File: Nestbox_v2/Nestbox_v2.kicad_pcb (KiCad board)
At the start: 2 copper layers, 85 x 60 mm, 93 parts, among them CON301 Micro_SD_Card, J201 BATT_CONN_01X02, J401 LB_DETECT_CONN_01X04, J402 PIR_CONN_01X04, J403 LB_LED_CONN_01X04, J601 LOAD_CELL_CONN_01X04, J701 RFID_CONN_01X05, P301 RX/TX, P302 TST/RST, P303 DEBUG_3V3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

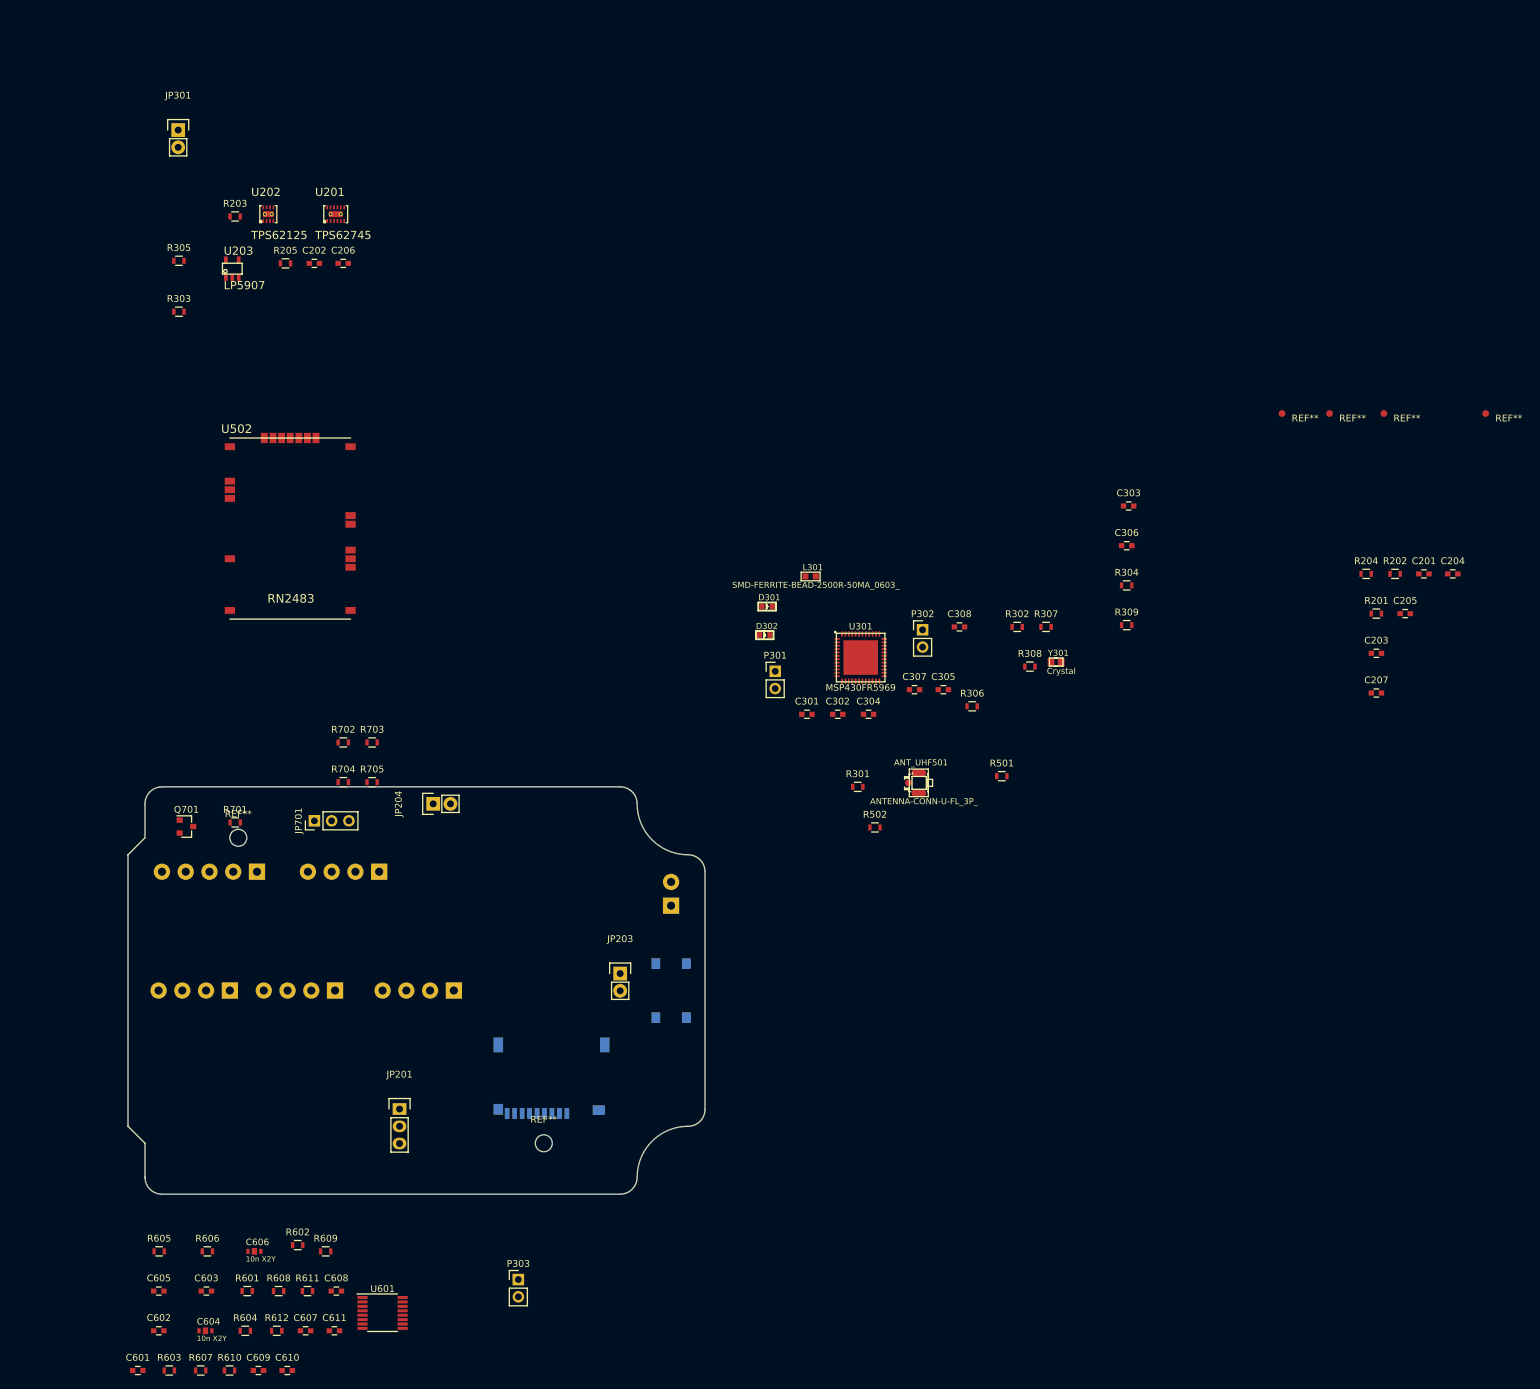
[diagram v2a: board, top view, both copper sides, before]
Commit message: all footprints assigned except mosfets; final connectors and their locatino, started component placement
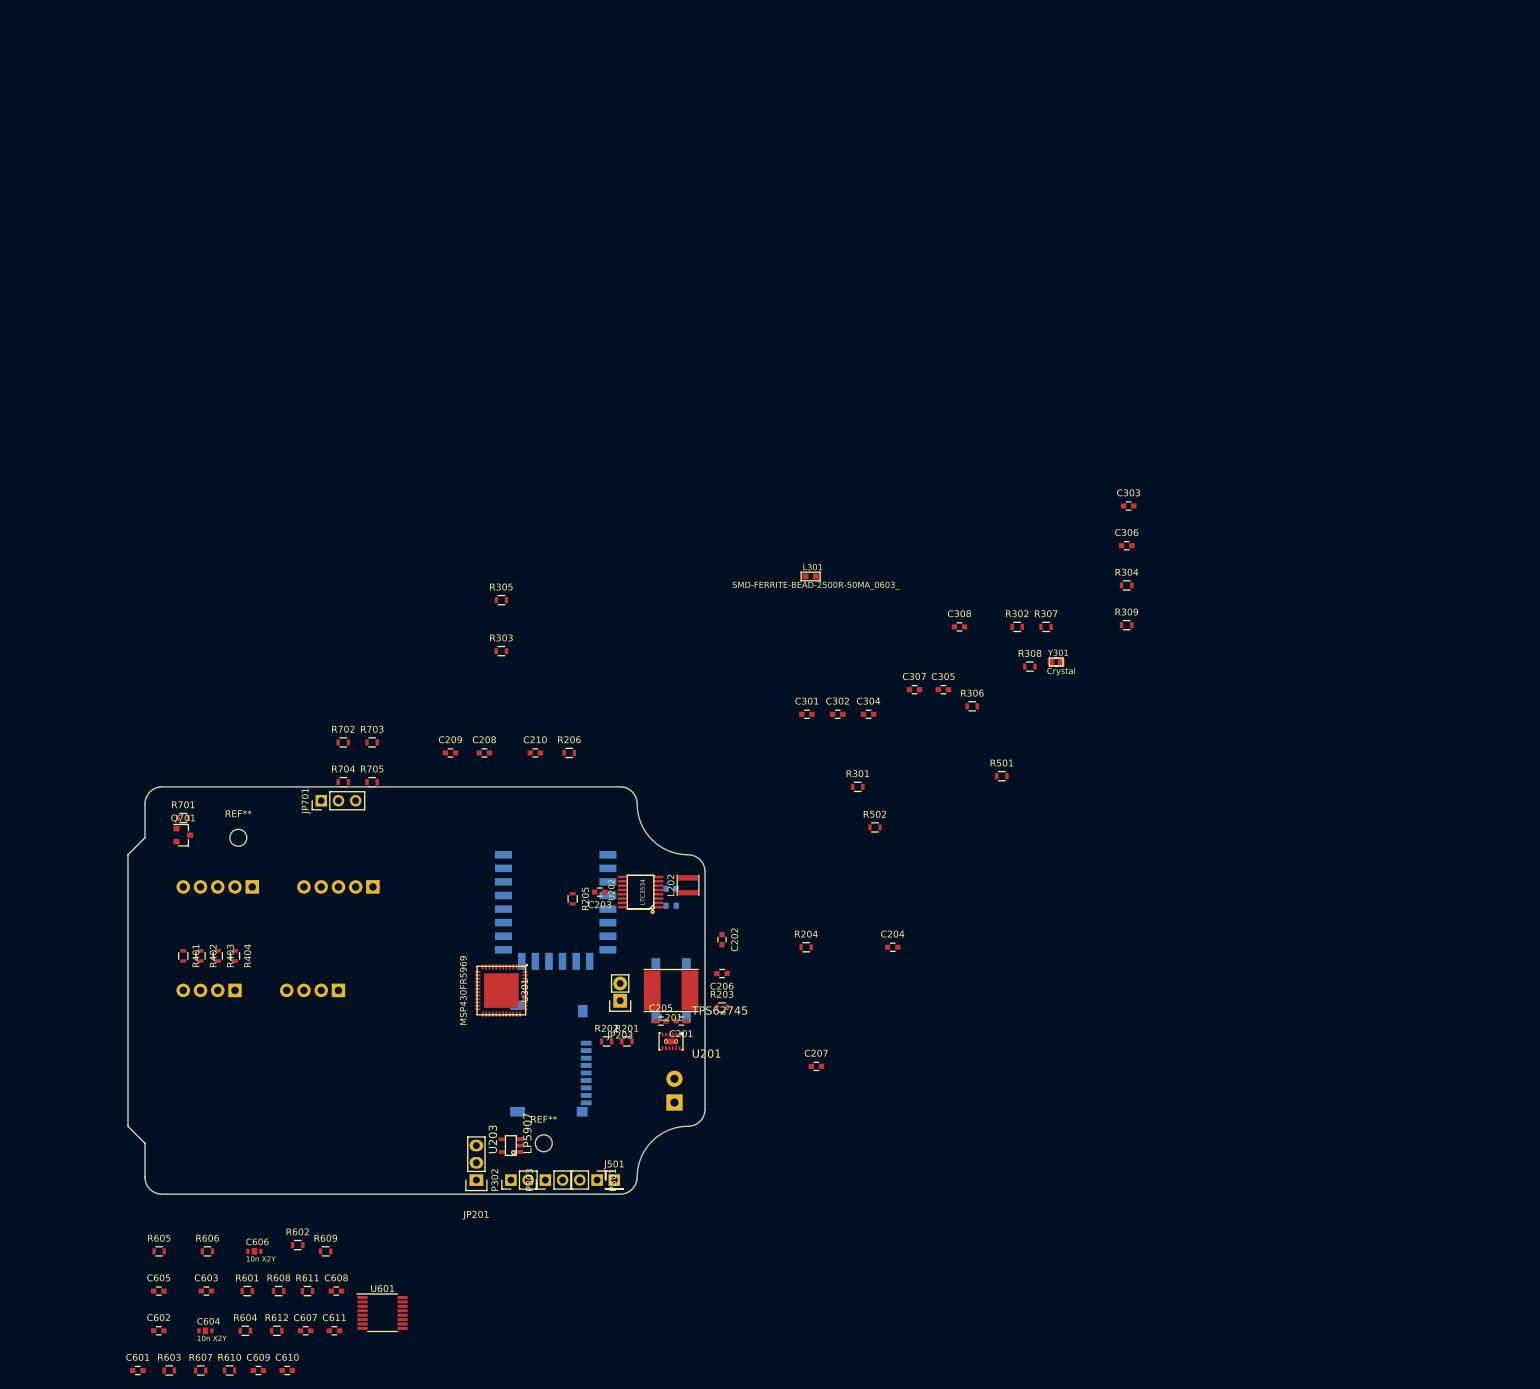
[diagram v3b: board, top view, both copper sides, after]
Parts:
- removed ANT_UHF501: ANTENNA-CONN-U-FL_3P_, SeeedOPL-Connector-2016:U-FL3P-SMD-2.6X2.6X1.0MM
- removed J403: LB_LED_CONN_01X04, Terminal_Blocks:TerminalBlock_Pheonix_PT-3.5mm_4pol
- removed JP204: Jumper_5V, Pin_Headers:Pin_Header_Straight_1x02
- removed JP301: Jumper, Pin_Headers:Pin_Header_Straight_1x02
- removed the REF** at (202.5, 72.5)
- removed the REF** at (209.5, 72.5)
- removed the REF** at (217.5, 72.5)
- removed the REF** at (232.5, 72.5)
- removed U502: RN2483, Octanis3:RN2483
- added C208: 330p, Capacitors_SMD:C_0603, F.Cu at (85.0, 122.5)
- added C209: 10p, Capacitors_SMD:C_0603, F.Cu at (80.0, 122.5)
- added C210: 33p, Capacitors_SMD:C_0603, F.Cu at (92.5, 122.5)
- added J501: CONN_01X01, Pin_Headers:Pin_Header_Straight_1x01_Pitch2.54mm, F.Cu at (104.1, 185.4)
- added L201: 4.7uH, Inductors:Inductor_Taiyo-Yuden_NR-60xx_HandSoldering, F.Cu at (112.5, 157.5)
- added L202: 5uH, Inductors:Inductor_Taiyo-Yuden_NR-30xx, F.Cu at (115.0, 142.0)
- added R206: 15k, Resistors_SMD:R_0603, F.Cu at (97.5, 122.5)
- added R401: DNP, Resistors_SMD:R_0603, F.Cu at (40.6, 152.4)
- added R402: DNP, Resistors_SMD:R_0603, F.Cu at (43.2, 152.4)
- added R403: DNP, Resistors_SMD:R_0603, F.Cu at (45.7, 152.4)
- added R404: DNP, Resistors_SMD:R_0603, F.Cu at (48.3, 152.4)
- added U501: ESP-12S, ESP8266:ESP-12E_SMD, B.Cu at (102.5, 137.5)
- D301, D302: moved to B.Cu
- J401, J601: footprint Terminal_Blocks:TerminalBlock_Pheonix_PT-3.5mm_4pol -> Terminal_Blocks:TerminalBlock_Pheonix_MPT-2.54mm_4pol
- J402: value PIR_CONN_01X04 -> CONN_01X05; footprint Terminal_Blocks:TerminalBlock_Pheonix_PT-3.5mm_4pol -> Terminal_Blocks:TerminalBlock_Pheonix_MPT-2.54mm_5pol
- J701: footprint Terminal_Blocks:TerminalBlock_Pheonix_PT-3.5mm_5pol -> Terminal_Blocks:TerminalBlock_Pheonix_MPT-2.54mm_5pol
- R203: value 1M -> 10k
- R204: value 210k -> 162k
- R205: value 1M1 -> 649k
- U202: value TPS62125 -> LTC3534; footprint Octanis3:WSON_2x2mm_8pin -> SeeedOPL-IC-2016:SSOP16-0.635-5X4MM
- moved R203 136.8 mm to (120.0, 160.0)
- moved U203 135.5 mm to (88.9, 180.3), turned to 90 degrees
- moved R202 135.0 mm to (103.0, 165.0)
- moved U201 131.9 mm to (113.0, 165.0), turned to 180 degrees
- moved C201 127.7 mm to (114.0, 162.0), turned to 180 degrees
- moved R201 127.1 mm to (106.0, 165.0)
- moved C205 125.0 mm to (111.0, 162.0)
- moved C203 119.7 mm to (102.0, 143.0), turned to 180 degrees
- moved C206 118.6 mm to (120.0, 155.0), turned to 180 degrees
- moved C202 116.3 mm to (120.0, 150.0), turned to 270 degrees
- moved U202 113.9 mm to (108.0, 143.0), turned to 90 degrees
- moved R205 102.7 mm to (98.0, 144.0), turned to 270 degrees
- moved P302 101.2 mm to (88.9, 185.4), turned to 90 degrees
- moved C204 99.2 mm to (145.1, 151.1)
- moved C207 99.2 mm to (133.9, 168.7)
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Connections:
- net /Communication/LORA_RX renamed Net-(P301-Pad2)
- net /PIR_OUT renamed /PIR_OUT1
- net Net-(J601-Pad2) renamed /Load_Cell/conn2
- net Net-(J601-Pad3) renamed /Load_Cell/conn3
- C206 pad 1: Net-(C206-Pad1) -> +5V
- C207 pad 1: Net-(C206-Pad1) -> +5V
- J201 pad 1: +BATT -> GND
- J201 pad 2: GND -> +BATT
- J402 pad 4: GND -> /PIR_OUT2
- R203 pad 1: +3V3 -> Net-(C210-Pad1)
- R203 pad 2: /Power/5V_PG -> +5V
- R204 pad 2: Net-(R204-Pad2) -> Net-(C209-Pad1)
- R205 pad 1: Net-(C206-Pad1) -> +5V
- R205 pad 2: Net-(R204-Pad2) -> Net-(C209-Pad1)
- R501 pad 2: (no net) -> Net-(R501-Pad2)
- U201 pad 3: (no net) -> Net-(L201-Pad1)
- U202 pad 2: +BATT -> /Control/5V_ENABLE
- U202 pad 3: /Control/5V_ENABLE -> GND
- U202 pad 4: (no net) -> GND
- U202 pad 5: Net-(R204-Pad2) -> Net-(L202-Pad1)
- U202 pad 6: Net-(C206-Pad1) -> Net-(L202-Pad2)
- U202 pad 7: (no net) -> GND
- U202 pad 8: /Power/5V_PG -> GND
- U301 pad 15: (no net) -> /Communication/ESP12_ENABLE
- U301 pad 24: (no net) -> /Communication/ESP12_RX
- U301 pad 25: (no net) -> /Communication/ESP12_TX
- U301 pad 39: (no net) -> /PIR_OUT2
- U301 pad 8: /Power/5V_PG -> /Power/5V_PWM

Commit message: ESP footprint to the essential and broke out programming pins
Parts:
- added J502: CONN_01X06, Pin_Headers:Pin_Header_Straight_1x06_Pitch2.54mm, F.Cu at (75.0, 197.6)
- added Q501: NTR3A052PZT1G, TO_SOT_Packages_SMD:SOT-23, F.Cu at (75.0, 197.6)
- added R503, R504, R505, R506: 10K, Resistors_SMD:R_0603, F.Cu at (75.0, 197.6)
- moved C204 60.1 mm to (90.0, 175.0), turned to 90 degrees
- moved C207 39.5 mm to (103.0, 144.0), turned to 270 degrees
- moved C209 35.3 mm to (108.0, 144.0), turned to 180 degrees
- moved C208 32.9 mm to (107.0, 147.0), turned to 90 degrees
- moved C202 32.0 mm to (100.0, 175.0), turned to 90 degrees
- moved C210 29.7 mm to (113.0, 144.0), turned to 90 degrees
- moved R206 27.1 mm to (109.0, 147.0), turned to 90 degrees
- moved R204 22.6 mm to (111.0, 144.0), turned to 270 degrees
- moved C206 22.0 mm to (101.0, 144.0), turned to 270 degrees
- moved L202 15.6 mm to (104.0, 131.0), turned to 180 degrees
- moved R203 14.8 mm to (113.0, 147.0), turned to 270 degrees
- moved R205 13.3 mm to (111.0, 147.0), turned to 90 degrees
- moved JP201 10.5 mm to (85.0, 175.0), turned to 0 degrees
- moved U203 8.11 mm to (95.0, 175.0)
- moved U501 7.57 mm to (95.0, 136.5)
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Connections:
- R501 pad 1: +3V3 -> /Communication/ESP12_VCC
- U501 pad 10: (no net) -> Net-(R504-Pad2)
- U501 pad 11: (no net) -> Net-(R506-Pad2)
- U501 pad 12: (no net) -> /Communication/DTR
- U501 pad 3: /Communication/ESP12_ENABLE -> /Communication/CTS

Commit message: finished component placement
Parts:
- added JP501: Jumper, Connect:GS2, F.Cu at (96.7, 140.5)
- added Q601: DMG2301L-7, TO_SOT_Packages_SMD:TSOT-23, F.Cu at (72.4, 163.2)
- added Q602: DMG3402L, TO_SOT_Packages_SMD:TSOT-23, F.Cu at (72.4, 168.3)
- added Q603: DMG2301L-7, TO_SOT_Packages_SMD:TSOT-23, F.Cu at (47.0, 163.2)
- added Q604: DMG3402L, TO_SOT_Packages_SMD:TSOT-23, F.Cu at (47.0, 168.3)
- added REF**: MountingHole_2.5mm, Mounting_Holes:MountingHole_2.5mm, F.Cu at (48.7, 180.0)
- C604, C606: footprint murata-filter:NFM18PS -> Octanis3:Capacitor_X2Y_603
- U501: footprint ESP8266:ESP-12E_SMD -> Octanis3:ESP-12E_SMD_UART_ONLY; moved to F.Cu
- moved R304 128.1 mm to (82.7, 181.5), turned to 90 degrees
- moved C303 114.9 mm to (98.2, 167.0)
- moved R302 109.2 mm to (86.7, 181.5), turned to 90 degrees
- moved C306 106.9 mm to (106.5, 170.0), turned to 270 degrees
- moved Y301 93.5 mm to (95.0, 166.0), turned to 270 degrees
- moved R501 89.3 mm to (72.7, 137.5)
- moved R309 83.9 mm to (111.0, 152.0)
- moved R305 81.8 mm to (80.7, 181.5), turned to 90 degrees
- moved C305 80.9 mm to (95.5, 170.5), turned to 180 degrees
- moved L301 75.0 mm to (98.3, 163.0)
- moved R301 74.5 mm to (88.7, 181.5), turned to 90 degrees
- moved R303 74.1 mm to (84.7, 181.5), turned to 90 degrees
- moved C304 72.3 mm to (95.5, 172.5), turned to 180 degrees
- moved C307 72.1 mm to (104.0, 170.0), turned to 270 degrees
- moved R308 71.4 mm to (107.8, 152.0)
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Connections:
- J502 pad 3: /Communication/ESP12_RX -> /Communication/RX
- J601 pad 1: /Load_Cell/EXC_B -> /Load_Cell/EXC_A
- J601 pad 4: /Load_Cell/EXC_A -> /Load_Cell/EXC_B
- J701 pad 2: /Control/RFID_CLK -> Net-(J701-Pad2)
- J701 pad 3: /Control/RFID_DATA -> Net-(J701-Pad3)
- R309 pad 1: (no net) -> /Control/DBG_Switch
- R401 pad 2: /Load_Cell/EXC_A -> /Load_Cell/EXC_B
- R404 pad 2: /Load_Cell/EXC_B -> /Load_Cell/EXC_A
- R601 pad 2: (no net) -> Net-(Q601-Pad3)
- R602 pad 2: (no net) -> Net-(Q603-Pad3)
- R702 pad 1: /RFID/RFID_VDD -> /Control/RFID_CLK
- R702 pad 2: /Control/RFID_CLK -> Net-(J701-Pad2)
- R703 pad 1: /Control/RFID_DATA -> Net-(J701-Pad3)
- R703 pad 2: /RFID/RFID_VDD -> /Control/RFID_DATA
- U301 pad 29: (no net) -> /Load_Cell/EXC_A_P
- U301 pad 30: (no net) -> /Load_Cell/EXC_A_N
- U301 pad 34: (no net) -> /Load_Cell/EXC_B_P
- U301 pad 35: (no net) -> /Load_Cell/EXC_B_N
- U501 pad 15: /Communication/ESP12_RX -> /Communication/RX
- U501 pad 8: +3V3 -> /Communication/ESP12_VCC
